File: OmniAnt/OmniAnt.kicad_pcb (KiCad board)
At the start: 2 copper layers, 77 parts, among them J1 Conn_01x02_Pin, J3 Connector, USB-TYPE-C-16P, J6 XT30PW-M, J7 XT30PW-M, J8 XT30PW-M, J9 XT30PW-M, Q1 NTMFS4C324NT1G, Q10 NTMFS4C324NT1G, Q11 NTMFS4C324NT1G, Q12 NTMFS4C324NT1G, Q2 NTMFS4C324NT1G, Q3 NTMFS4C324NT1G, Q4 NTMFS4C324NT1G, Q5 NTMFS4C324NT1G, Q6 NTMFS4C324NT1G, Q7 NTMFS4C324NT1G, Q8 NTMFS4C324NT1G, Q9 NTMFS4C324NT1G, U1 ESP32-S3-WROOM-1, U2 TPSM53603RDA, U3 MCF8329A1IREER, U4 USBLC6-2P6, U5 MCF8329A1IREER

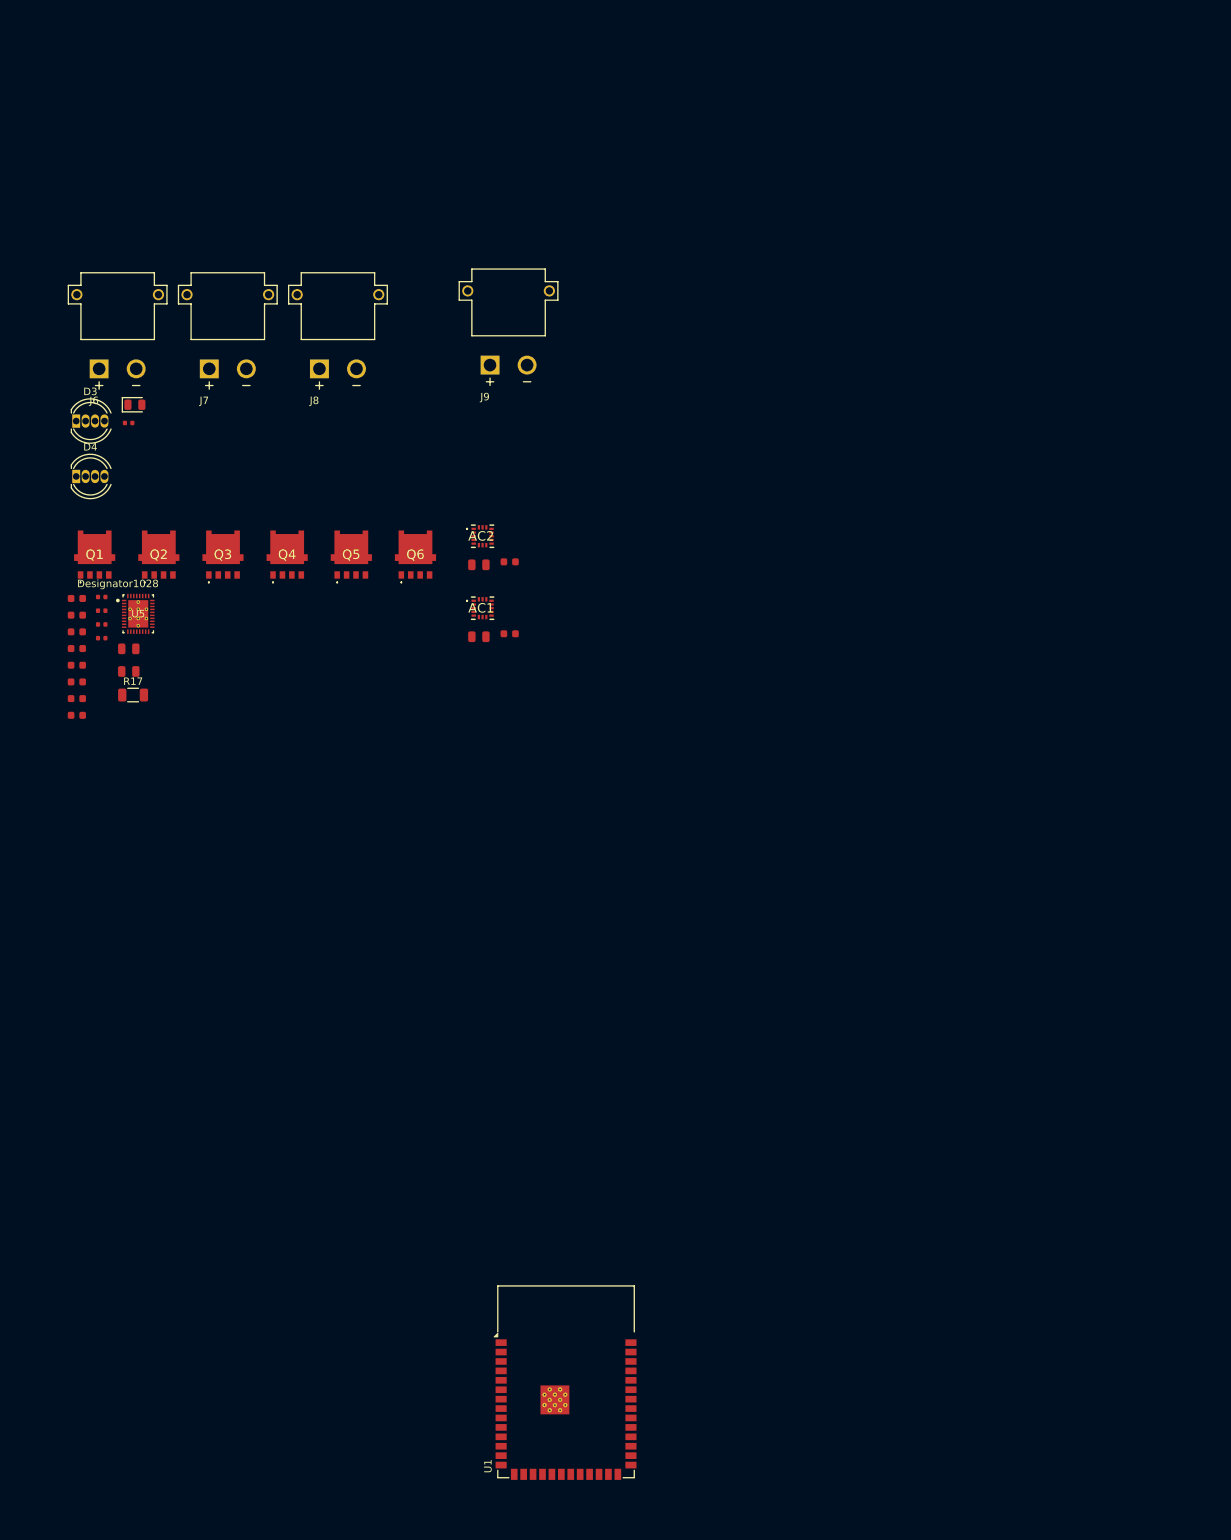
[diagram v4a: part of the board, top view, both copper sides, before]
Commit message: added a link to the motor controller datasheet and changed the connector footprint for the RC interface.
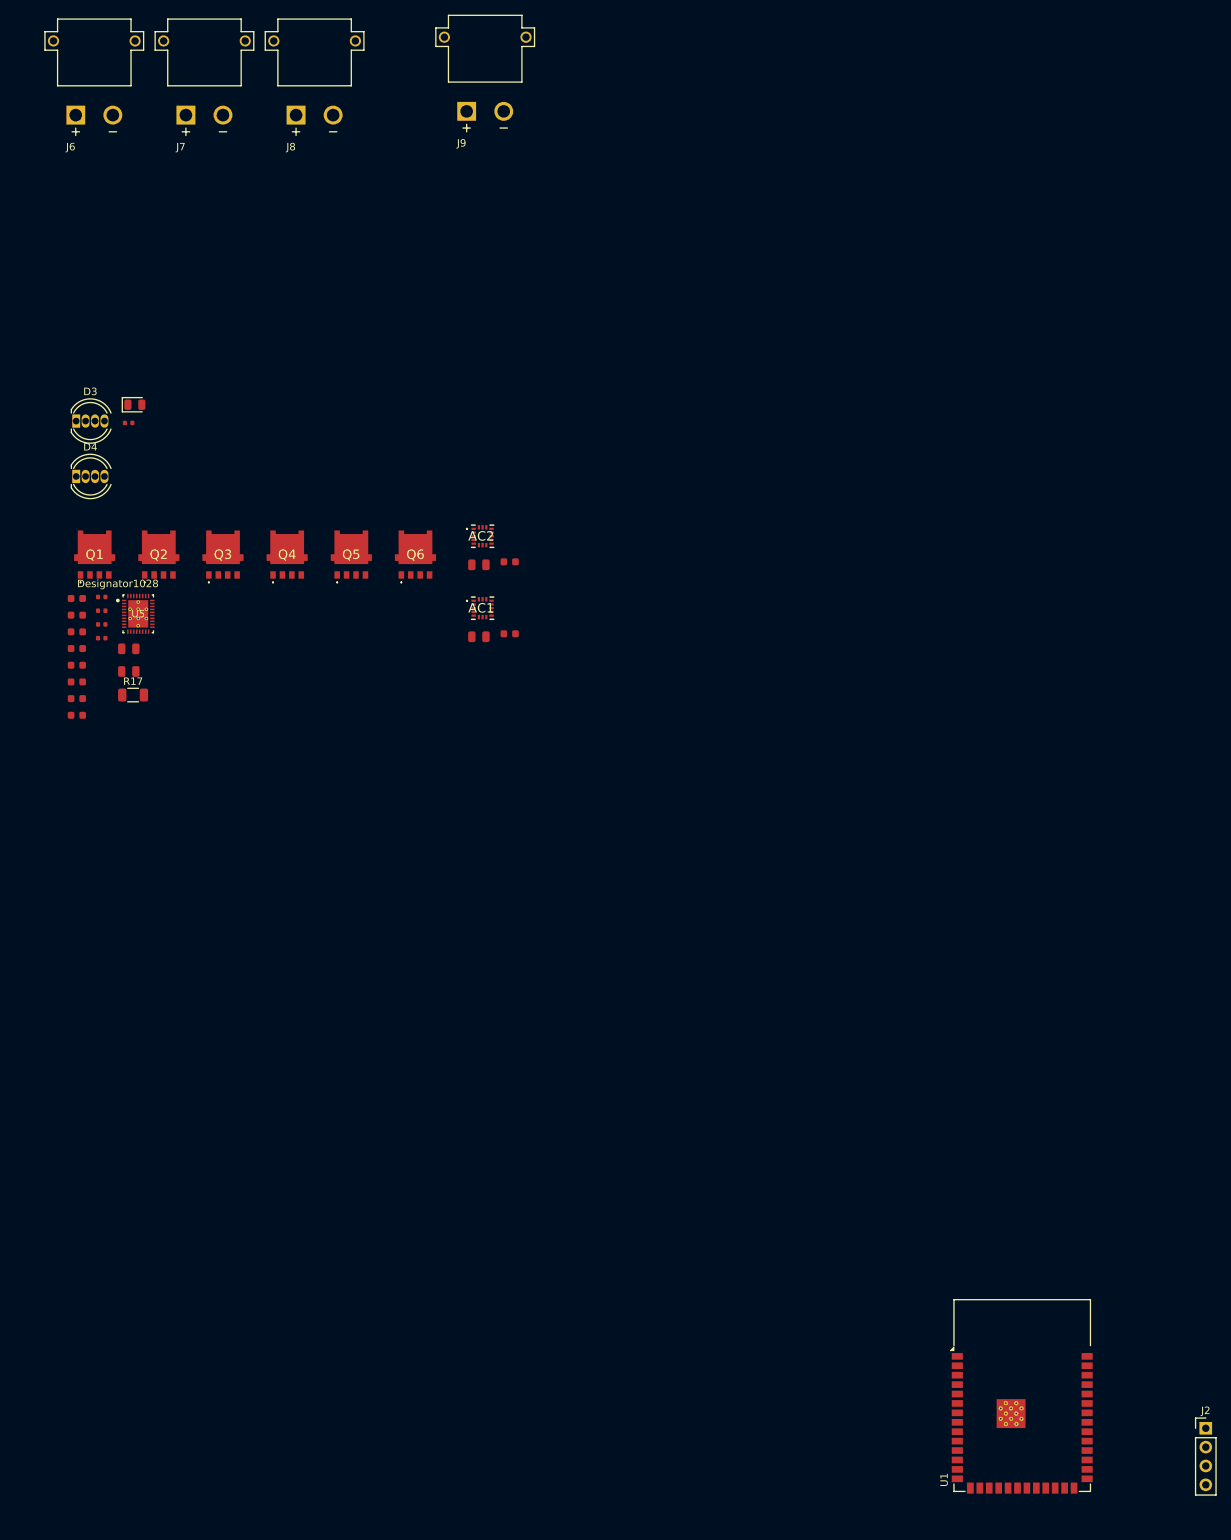
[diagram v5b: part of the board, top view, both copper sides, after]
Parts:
- added J2: Conn_01x04_Pin, Connector_PinHeader_2.54mm:PinHeader_1x04_P2.54mm_Vertical, F.Cu at (203.5, 90.0)
- moved U1 61.5 mm to (178.8, 85.6)
- moved J9 34.4 mm to (106.3, -97.5)
- moved J6 34.4 mm to (53.6, -97.0)
- moved J7 34.4 mm to (68.5, -97.0)
- moved J8 34.4 mm to (83.3, -97.0)

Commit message: fixed all the schematic errors.
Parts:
- removed the C12 at (58.3, -15.0)
- removed the C13 at (58.3, -12.0)
- removed the C16 at (51.3, -17.3)
- removed the C3 at (51.3, -21.8)
- removed the C4 at (109.7, -26.8)
- removed the C5 at (51.3, -19.6)
- removed the C6 at (105.5, -26.4)
- removed the Q1 at (53.7, -27.8)
- removed the Q2 at (62.4, -27.8)
- removed the Q3 at (71.0, -27.8)
- removed the Q4 at (79.7, -27.8)
- removed the Q5 at (88.3, -27.8)
- removed the Q6 at (97.0, -27.8)
- removed the R7 at (54.6, -22.0)
- removed the R8 at (54.6, -20.2)
- added C19: 10uF, PCM_JLCPCB:C_0805, F.Cu at (-37.6, -65.3)
- added C20: 10uF, PCM_JLCPCB:C_0805, F.Cu at (-37.6, -62.2)
- added C21: 100nF, PCM_JLCPCB:C_0603, F.Cu at (-44.6, -67.6)
- added C22: 1uF, PCM_JLCPCB:C_0603, F.Cu at (-44.6, -65.3)
- added C23: 470pF, PCM_JLCPCB:C_0603, F.Cu at (-44.6, -63.1)
- added C29: 100nF, PCM_JLCPCB:C_0603, F.Cu at (-58.6, -47.4)
- added C30: 10uF, PCM_JLCPCB:C_0805, F.Cu at (-62.8, -47.0)
- added J8: MR30PW-FB, Footprints:MR30PWFB, F.Cu at (63.5, 96.0)
- added J9: MR30PW-FB, Footprints:MR30PWFB, F.Cu at (-52.2, -57.9)
- added Q10: NTMFS4C324NT1G, Footprints:NVMFS5C442NLWFAFT1G, F.Cu at (-34.7, -78.0)
- added Q11: NTMFS4C324NT1G, Footprints:NVMFS5C442NLWFAFT1G, F.Cu at (-26.1, -78.0)
- added Q12: NTMFS4C324NT1G, Footprints:NVMFS5C442NLWFAFT1G, F.Cu at (-17.4, -78.0)
- added Q7: NTMFS4C324NT1G, Footprints:NVMFS5C442NLWFAFT1G, F.Cu at (-60.7, -78.0)
- added Q8: NTMFS4C324NT1G, Footprints:NVMFS5C442NLWFAFT1G, F.Cu at (-52.0, -78.0)
- added Q9: NTMFS4C324NT1G, Footprints:NVMFS5C442NLWFAFT1G, F.Cu at (-43.4, -78.0)
- added R14: 10kΩ, PCM_JLCPCB:R_0402, F.Cu at (-41.2, -72.3)
- added R18: 2m, Resistor_SMD:R_1206_3216Metric, F.Cu at (-37.0, -59.1)
- C18: value 470pF -> 1uF
- R15: value 5.1kΩ -> 10kΩ
- R17: value 2m -> 5.1kΩ; footprint Resistor_SMD:R_1206_3216Metric -> PCM_JLCPCB:R_0402
- moved AC2 169.5 mm to (-62.3, -50.8)
- moved R17 115.6 mm to (-41.2, -66.7)
- moved C17 111.5 mm to (-44.6, -72.1)
- moved C18 111.5 mm to (-44.6, -69.8)
- moved R15 109.1 mm to (-41.2, -70.4)
- moved R16 109.1 mm to (-41.2, -68.6)
- moved C26 108.2 mm to (-44.6, -56.3)
- moved U5 108.2 mm to (-36.3, -70.0)
- moved C24 108.2 mm to (-44.6, -60.8)
- moved C25 108.2 mm to (-44.6, -58.6)
- renumbered C23 to C1, C19 to C10, C20 to C11, C21 to C12, C27 to C13, C28 to C14, C29 to C15, C30 to C16, C9 to C2, C2 to C27, C1 to C28, C10 to C3, C15 to C4, C22 to C5, C7 to C6, C8 to C7, C11 to C8, C14 to C9, D2 to D1, D4 to D2, D1 to D4, J3 to J1, J1 to J2, J2 to J3, J6 to J4, J7 to J5, J8 to J6, J9 to J7, Q7 to Q1, Q8 to Q2, Q9 to Q3, Q10 to Q4, Q11 to Q5, Q12 to Q6, R14 to R1, R6 to R10, R10 to R11, R9 to R12, R18 to R13, R13 to R2, R1 to R3, R3 to R4, R2 to R6, R12 to R7, R11 to R8, R4 to R9, U4 to U1, U1 to U3, U3 to U4
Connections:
- net Net-(J6-PadN) renamed /Batt_3S
- net Net-(J7-PadN) renamed /Batt_2S
- net Net-(J8-PadN) renamed /Batt_1S
- net Net-(Q1-S_1) renamed /Motor2/PhaseA
- net Net-(Q10-D_1) renamed /Motor1/PhaseB
- net Net-(Q11-S_1) renamed /Motor1/PhaseC
- net Net-(Q7-S_1) renamed /Motor1/PhaseA
- AC1 pad 10: Net-(AC1-GND_2) -> GND
- AC1 pad 12: Net-(AC1-GND_2) -> GND
- AC1 pad 13: Net-(AC1-GND_2) -> GND
- AC2 pad 10: Net-(AC2-GND_2) -> GND
- AC2 pad 12: Net-(AC2-GND_2) -> GND
- AC2 pad 13: Net-(AC2-GND_2) -> GND
- C10 pad 1: /Motor1/Batt -> /Batt
- C11 pad 1: /Motor1/Batt -> /Batt
- C12 pad 1: /Motor1/3.3V -> +3.3V
- C17 pad 1: /Motor2/3.3V -> Net-(U5-AVDD)
- C18 pad 1: Net-(U5-CPH) -> Net-(U5-DVDD)
- C18 pad 2: Net-(U5-CPL) -> GND
- C27 pad 2: Net-(AC1-GND_2) -> GND
- C28 pad 2: Net-(AC1-GND_2) -> GND
- Q1 pad 5: /Motor1/Batt -> /Batt
- Q1 pad 6: /Motor1/Batt -> /Batt
- Q1 pad 7: /Motor1/Batt -> /Batt
- Q1 pad 8: /Motor1/Batt -> /Batt
- Q1 pad 9: /Motor1/Batt -> /Batt
- Q3 pad 5: /Motor1/Batt -> /Batt
- Q3 pad 6: /Motor1/Batt -> /Batt
- Q3 pad 7: /Motor1/Batt -> /Batt
- Q3 pad 8: /Motor1/Batt -> /Batt
- Q3 pad 9: /Motor1/Batt -> /Batt
- Q5 pad 5: /Motor1/Batt -> /Batt
- Q5 pad 6: /Motor1/Batt -> /Batt
- Q5 pad 7: /Motor1/Batt -> /Batt
- Q5 pad 8: /Motor1/Batt -> /Batt
- Q5 pad 9: /Motor1/Batt -> /Batt
- R15 pad 1: +3.3V -> GND
- R15 pad 2: Net-(U5-FAULT_N) -> Net-(U5-DIR)
- R16 pad 2: Net-(U5-FG) -> Net-(U5-FAULT_N)
- R17 pad 1: GND -> +3.3V
- R17 pad 2: /Motor2/LSS -> Net-(U5-FG)
- U4 pad 2: /Motor1/3.3V -> +3.3V
- U4 pad 29: /Motor1/I2C_SDA -> /I2C_SDA
- U4 pad 30: /Motor1/I2C_SCL -> /I2C_SCL
- U4 pad 5: /Motor1/Batt -> /Batt
- U5 pad 2: /Motor2/3.3V -> +3.3V
- U5 pad 29: /Motor2/I2C_SDA -> /I2C_SDA
- U5 pad 30: /Motor2/I2C_SCL -> /I2C_SCL
- U5 pad 5: /Motor2/Batt -> /Batt
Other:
- copper layers 2 -> 4

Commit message: I started to work on the rough placement.
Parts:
- added J10: Conn_01x01, Connector_Wire:SolderWire-0.25sqmm_1x01_D0.65mm_OD1.7mm, F.Cu at (35.6, 99.2)
- added J11: Conn_01x01, Connector_Wire:SolderWire-0.25sqmm_1x01_D0.65mm_OD1.7mm, F.Cu at (273.9, 23.3)
- added J12: Conn_01x01, Connector_Wire:SolderWire-0.25sqmm_1x01_D0.65mm_OD1.7mm, F.Cu at (35.6, 103.8)
- added J13: Conn_01x01, Connector_Wire:SolderWire-0.25sqmm_1x01_D0.65mm_OD1.7mm, F.Cu at (273.9, 15.8)
- J8, J9: value MR30PW-FB -> Conn_01x01; footprint Footprints:MR30PWFB -> Connector_Wire:SolderWire-0.25sqmm_1x01_D0.65mm_OD1.7mm
- moved Q7 357.6 mm to (279.7, 31.5), turned to -90 degrees
- moved Q9 338.8 mm to (279.7, 24.0), turned to -90 degrees
- moved Q8 338.1 mm to (268.0, 30.9), turned to -90 degrees
- moved J9 338.0 mm to (273.9, 30.9), turned to 180 degrees
- moved Q11 320.0 mm to (279.7, 16.4), turned to -90 degrees
- moved Q10 319.2 mm to (268.0, 23.3), turned to -90 degrees
- moved C17 317.9 mm to (257.5, 27.1)
- moved C25 313.0 mm to (254.8, 32.8), turned to -90 degrees
- moved R17 311.5 mm to (256.3, 25.6), turned to -90 degrees
- moved C26 310.5 mm to (252.9, 32.6), turned to -90 degrees
- moved R15 309.9 mm to (254.0, 24.0), turned to -90 degrees
- moved C24 309.5 mm to (250.7, 31.9), turned to -90 degrees
- moved R14 309.4 mm to (252.8, 24.0), turned to -90 degrees
- moved C18 309.2 mm to (249.8, 24.9), turned to 180 degrees
- moved C21 309.1 mm to (249.6, 27.5), turned to 180 degrees
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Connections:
- C15 pad 2: Net-(U4-SHC) -> /Motor1/PhaseC
- C16 pad 2: Net-(U4-SHB) -> /Motor1/PhaseB
- C25 pad 2: Net-(U5-SHC) -> /Motor2/PhaseC
- C26 pad 2: Net-(U5-SHB) -> /Motor2/PhaseB
- U4 pad 14: Net-(U4-SHB) -> /Motor1/PhaseB
- U4 pad 18: Net-(U4-SHC) -> /Motor1/PhaseC
- U5 pad 14: Net-(U5-SHB) -> /Motor2/PhaseB
- U5 pad 18: Net-(U5-SHC) -> /Motor2/PhaseC

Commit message: Major progress on the motor driver layout. Lots of learning with how to draw traces and pours.
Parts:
- added H1: MountingHole, MountingHole:MountingHole_4.3mm_M4_DIN965, F.Cu at (202.1, 23.8)
- added H2: MountingHole, MountingHole:MountingHole_3mm, F.Cu at (95.0, 17.1)
- added H3: MountingHole, MountingHole:MountingHole_3mm, F.Cu at (95.0, 27.8)
- added H4: MountingHole, MountingHole:MountingHole_3mm, F.Cu at (305.5, 21.0)
- added H5: MountingHole, MountingHole:MountingHole_3mm, F.Cu at (305.5, 28.5)
- added J14: Conn_01x01, Connector_Wire:SolderWire-1.5sqmm_1x01_D1.7mm_OD3mm, F.Cu at (217.2, 29.5)
- added J15: Conn_01x01, Connector_Wire:SolderWire-1.5sqmm_1x01_D1.7mm_OD3mm, F.Cu at (214.4, 29.5)
- added J16: Conn_01x01, Connector_Wire:SolderWire-1.5sqmm_1x01_D1.7mm_OD3mm, F.Cu at (203.4, 29.5)
- added J17: Conn_01x01, Connector_Wire:SolderWire-1.5sqmm_1x01_D1.7mm_OD3mm, F.Cu at (200.6, 29.5)
- added J18: Conn_01x01, Connector_Wire:SolderWire-1.5sqmm_1x01_D1.7mm_OD3mm, F.Cu at (189.6, 29.5)
- added J19: Conn_01x01, Connector_Wire:SolderWire-1.5sqmm_1x01_D1.7mm_OD3mm, F.Cu at (186.8, 29.5)
- added J20: Conn_01x01, Connector_Wire:SolderWire-1.5sqmm_1x01_D1.7mm_OD3mm, F.Cu at (227.5, 25.7)
- added J21: Conn_01x01, Connector_Wire:SolderWire-1.5sqmm_1x01_D1.7mm_OD3mm, F.Cu at (176.7, 25.9)
- added J22: Conn_01x01, Connector_Wire:SolderWire-1.5sqmm_1x01_D1.7mm_OD3mm, F.Cu at (181.2, 25.9)
- added J23: Conn_01x01, Connector_Wire:SolderWire-0.25sqmm_1x01_D0.65mm_OD1.7mm, F.Cu at (114.0, 44.8)
- added J24: Conn_01x01, Connector_Wire:SolderWire-1.5sqmm_1x01_D1.7mm_OD3mm, F.Cu at (223.4, 25.7)
- added J25: Conn_01x01, Connector_Wire:SolderWire-0.25sqmm_1x01_D0.65mm_OD1.7mm, F.Cu at (263.0, 15.4)
- added J26: Conn_01x01, Connector_Wire:SolderWire-0.25sqmm_1x01_D0.65mm_OD1.7mm, F.Cu at (114.0, 48.7)
- added J27: Conn_01x01, Connector_Wire:SolderWire-0.25sqmm_1x01_D0.65mm_OD1.7mm, F.Cu at (263.0, 23.0)
- added J28: Conn_01x01, Connector_Wire:SolderWire-0.25sqmm_1x01_D0.65mm_OD1.7mm, F.Cu at (114.0, 52.6)
- added J29: Conn_01x01, Connector_Wire:SolderWire-0.25sqmm_1x01_D0.65mm_OD1.7mm, F.Cu at (263.0, 30.5)
- added J30: Conn_01x01, Connector_Wire:SolderWire-0.25sqmm_1x01_D0.65mm_OD1.7mm, F.Cu at (114.0, 56.5)
- added J31: Conn_01x01, Connector_Wire:SolderWire-0.25sqmm_1x01_D0.65mm_OD1.7mm, F.Cu at (270.1, 49.0)
- added J32: Conn_01x01, Connector_Wire:SolderWire-0.25sqmm_1x01_D0.65mm_OD1.7mm, F.Cu at (118.3, 44.8)
- added J33: Conn_01x01, Connector_Wire:SolderWire-0.25sqmm_1x01_D0.65mm_OD1.7mm, F.Cu at (275.3, 49.0)
- added J34: Conn_01x01, Connector_Wire:SolderWire-0.25sqmm_1x01_D0.65mm_OD1.7mm, F.Cu at (118.3, 48.7)
- added J35: Conn_01x01, Connector_Wire:SolderWire-0.25sqmm_1x01_D0.65mm_OD1.7mm, F.Cu at (275.3, 52.9)
- added J36: Conn_01x01, Connector_Wire:SolderWire-1.5sqmm_1x01_D1.7mm_OD3mm, F.Cu at (118.3, 52.6)
- added J37: Conn_01x01, Connector_Wire:SolderWire-1.5sqmm_1x01_D1.7mm_OD3mm, F.Cu at (257.1, 16.5)
- added J38: Conn_01x01, Connector_Wire:SolderWire-1.5sqmm_1x01_D1.7mm_OD3mm, F.Cu at (119.8, 57.6)
- added J39: Conn_01x01, Connector_Wire:SolderWire-1.5sqmm_1x01_D1.7mm_OD3mm, F.Cu at (287.1, 24.2)
- moved C1 351.8 mm to (236.4, 29.9), turned to 90 degrees
- moved D1 334.8 mm to (231.1, 30.3), turned to -90 degrees
- moved U1 293.4 mm to (234.7, 30.8), turned to 90 degrees
- moved U2 283.7 mm to (234.8, 21.7), turned to 180 degrees
- moved R8 278.7 mm to (166.7, 32.3)
- moved R7 276.6 mm to (164.6, 32.3), turned to 180 degrees
- moved C5 266.8 mm to (150.3, 13.8), turned to 90 degrees
- moved C4 266.4 mm to (150.3, 16.6), turned to -90 degrees
- moved R3 261.6 mm to (148.8, 15.9)
- moved C6 261.5 mm to (148.7, 13.8), turned to 90 degrees
- moved C13 255.8 mm to (140.6, 19.4), turned to 180 degrees
- moved C11 253.3 mm to (137.8, 20.3)
- moved C12 253.0 mm to (137.8, 21.5)
- moved C8 252.8 mm to (137.6, 22.9)
- moved C14 252.1 mm to (136.7, 15.9), turned to 90 degrees
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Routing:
- net /Motor2/LSS: track 0.00 -> 7.70 mm
- net Net-(Q9-G): track 0.00 -> 4.14 mm
- net GND: track 0.00 -> 4.11 mm
- net Net-(Q10-G): track 0.00 -> 3.97 mm
- net /Motor2/PhaseB: track 0.00 -> 3.81 mm
- net Net-(J1-D--PadA7): track 0.00 -> 2.48 mm
- net Net-(J1-D+-PadA6): track 0.00 -> 2.48 mm
- net /SPI1_SCK: track 0.00 -> 2.16 mm
- net Net-(U5-AVDD): track 0.00 -> 1.65 mm
- net Net-(U5-BSTB): track 0.00 -> 1.65 mm
- net Net-(U5-BSTC): track 0.00 -> 1.65 mm
- net Net-(U5-FG): track 0.00 -> 1.42 mm
- net Net-(J1-CC2): track 0.00 -> 1.40 mm
- net Net-(J1-CC1): track 0.00 -> 1.40 mm
- net /Motor2_PWM: track 0.00 -> 1.40 mm, vias 0 -> 1
- added copper zone on B.Cu, net /Batt
- added copper zone on F.Cu, net /Batt
- added copper zone on In1.Cu, net /Batt
- added copper zone on In2.Cu, net /Batt
- added copper zone on B.Cu, net /Motor2/LSS
- added copper zone on F.Cu, net /Motor2/LSS
- added copper zone on In1.Cu, net /Motor2/LSS
- added copper zone on In2.Cu, net /Motor2/LSS
- added copper zone on B.Cu, net /Motor2/PhaseA
- added copper zone on F.Cu, net /Motor2/PhaseA
- added copper zone on In1.Cu, net /Motor2/PhaseA
- added copper zone on In2.Cu, net /Motor2/PhaseA
- added copper zone on B.Cu, net /Motor2/PhaseB
- added copper zone on F.Cu, net /Motor2/PhaseB
- added copper zone on In1.Cu, net /Motor2/PhaseB
- added copper zone on In2.Cu, net /Motor2/PhaseB
- added copper zone on B.Cu, net /Motor2/PhaseC
- added copper zone on F.Cu, net /Motor2/PhaseC
- added copper zone on In1.Cu, net /Motor2/PhaseC
- added copper zone on In2.Cu, net /Motor2/PhaseC
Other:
- board text added: "TODO: Add solder wire connections for the busbar wires. Add mounting / locating holes for the motor. Add boxes to represent the batteries."
